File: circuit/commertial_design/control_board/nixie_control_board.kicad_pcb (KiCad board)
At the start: 2 copper layers, 200 x 65.3 mm, 75 parts, among them CON1 BARREL_JACK, IC1 ATMEGA328P-A, P1 CONN_01X08, P2 CONN_02X03, P3 CONN_01X12, P4 CONN_01X04, P5 BLUETOOTH_SJ, P6 CONN_02X03, Q1 2SB647, Q2 2SK3611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

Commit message: Add some marks
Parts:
- added REF**: Symbol_HighVoltage_Type2_CopperTop_VerySmall, warning:warning, B.Cu at (122.0, 124.3)
- added REF**: Pin_Header_Straight_2x03, Pin_Headers:Pin_Header_Straight_2x03, F.Cu at (178.0, 85.6)
- added REF**: Pin_Header_Straight_2x06, Pin_Headers:Pin_Header_Straight_2x06, F.Cu at (157.7, 85.6)
- added REF**: Pin_Header_Straight_2x04, Pin_Headers:Pin_Header_Straight_2x04, F.Cu at (142.4, 85.6)
- added REF**: Symbol_HighVoltage_Type2_CopperTop_VerySmall, warning:warning, F.Cu at (122.3, 125.5)
- moved C10 7.96 mm to (77.6, 106.9), turned to 90 degrees
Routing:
- net /power_supply/12V: track 61.5 -> 86.4 mm
- net Net-(P1-Pad5): track 17.8 -> 9.62 mm
- net /RTC/GND: track 894.3 -> 893.4 mm
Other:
- board text added: "Designed by Shengwen Cheng (2013 - 2016)"
- board text removed: "Designed by Shengwen Cheng"
- board text removed: "NIXIE CLOCK CONTROL BOARD"

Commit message: Push the forgotten file
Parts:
- removed R13, R14: 330ohm, Resistors_SMD:R_1206_HandSoldering
- removed the REF** at (122.0, 124.3)
- removed the REF** at (178.0, 85.6)
- removed the REF** at (122.3, 125.5)
- BT1: value CR1220 -> CR2032
- C6: value 33v/250v -> 33uf/250v
- P2: value CONN_02X03 -> CONN_02X01; footprint SMD_PIN_2_BY_3_REVERSE:SMD_PIN_2_BY_3_REVERSE -> Pin_Headers:Pin_Header_Straight_2x01
- Q3, Q4: value Q_NPN_EBC -> MPSA42
- R10: value R -> 33K ohm
- R11: value R -> 33k ohm
- R7: value 760 ohm -> 750 ohm
- R9: value 18k ohm -> 5.1k ohm
- moved R19 6.25 mm to (217.1, 113.5)
- moved R18 6.20 mm to (217.0, 111.1)
- moved C13 1.87 mm to (223.0, 110.2), turned to 270 degrees
- turned C15 to 0 degrees
- turned P2 to 90 degrees
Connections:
- IC1 pad 1: Search_button -> dfplayer_state
- IC1 pad 12: Digit_A0 -> MP3_RX
- IC1 pad 13: dfplayer_state -> MP3_TX
- IC1 pad 19: dfplayer_pre -> (no net)
- IC1 pad 2: Adjust_button -> (no net)
- IC1 pad 22: dfplayer_next -> (no net)
- IC1 pad 25: MP3_TX -> (no net)
- IC1 pad 26: MP3_RX -> Digit_A0
- R18 pad 2: MP3_RX -> MP3_TX
- R19 pad 2: MP3_TX -> MP3_RX
- U18 pad 11: dfplayer_pre -> (no net)
- U18 pad 9: dfplayer_next -> (no net)
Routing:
- net dfplayer_state: track 110.9 -> 42.2 mm, vias 2 -> 1
- net dfplayer_pre: track 67.3 -> 0.00 mm, vias 2 -> 0
- net dfplayer_next: track 56.4 -> 0.00 mm, vias 1 -> 0
- net Adjust_button: track 55.9 -> 0.00 mm, vias 2 -> 0
- net Search_button: track 53.9 -> 0.00 mm, vias 2 -> 0
- net MP3_RX: track 3.88 -> 22.4 mm, vias 0 -> 2
- net MP3_TX: track 4.61 -> 22.9 mm, vias 0 -> 2
- net Digit_A0: track 76.8 -> 91.8 mm, vias 1 -> 0
- net /RTC/I2C_SDA: track 51.8 -> 43.1 mm
- net /RTC/GND: track 893.4 -> 887.4 mm
- net /RTC/5V: track 367.9 -> 373.7 mm, vias 3 -> 5
- net Net-(R19-Pad1): track 13.3 -> 7.65 mm
- net Net-(R18-Pad1): track 13.3 -> 7.66 mm
- net Reset: track 58.8 -> 62.4 mm
- net left_comma: track 52.6 -> 55.1 mm, vias 1 -> 3
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
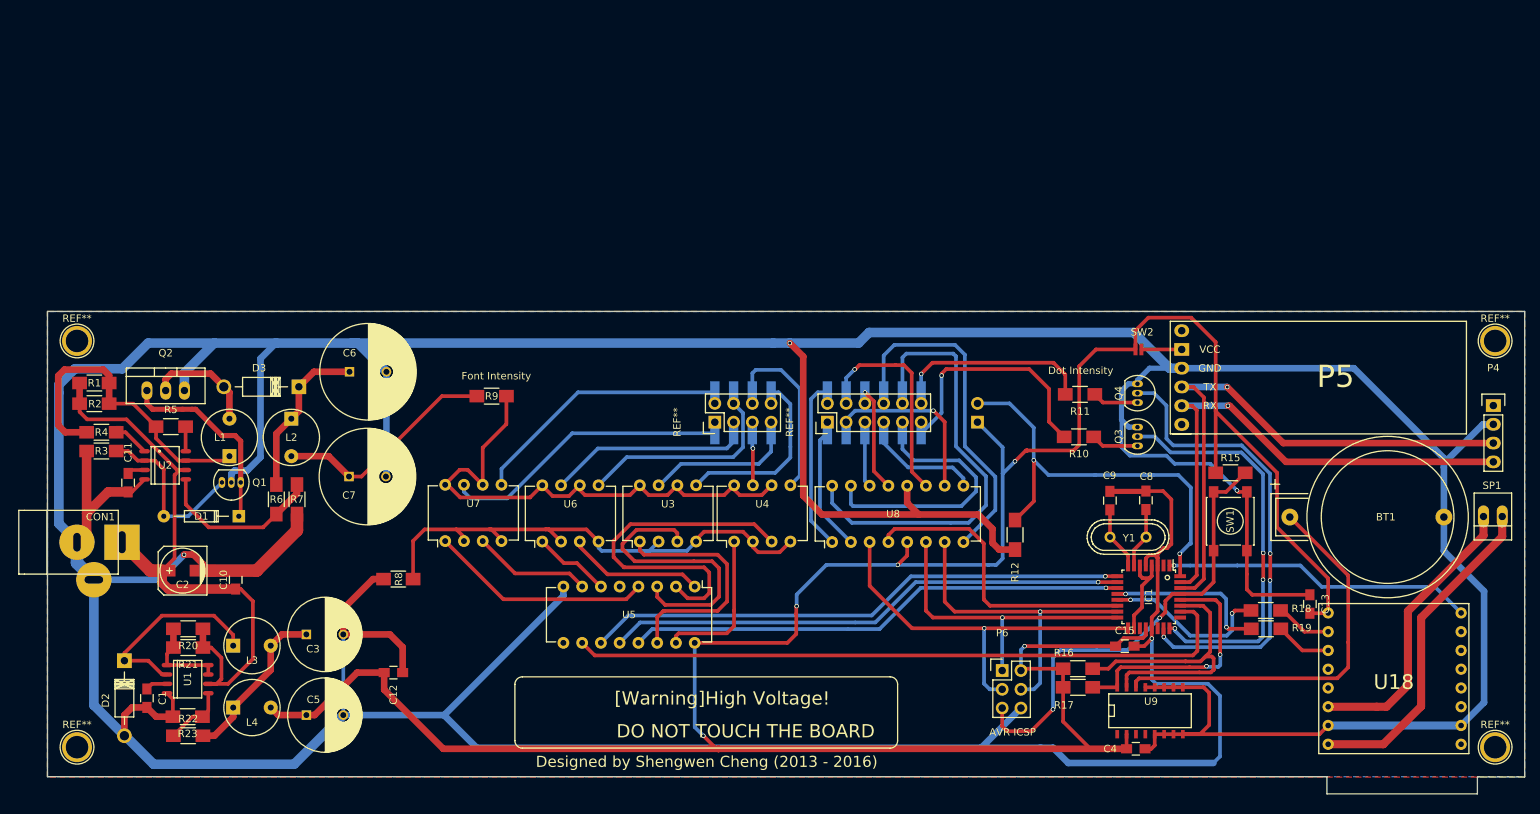
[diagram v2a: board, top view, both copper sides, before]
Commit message: Add ratio extender circuit
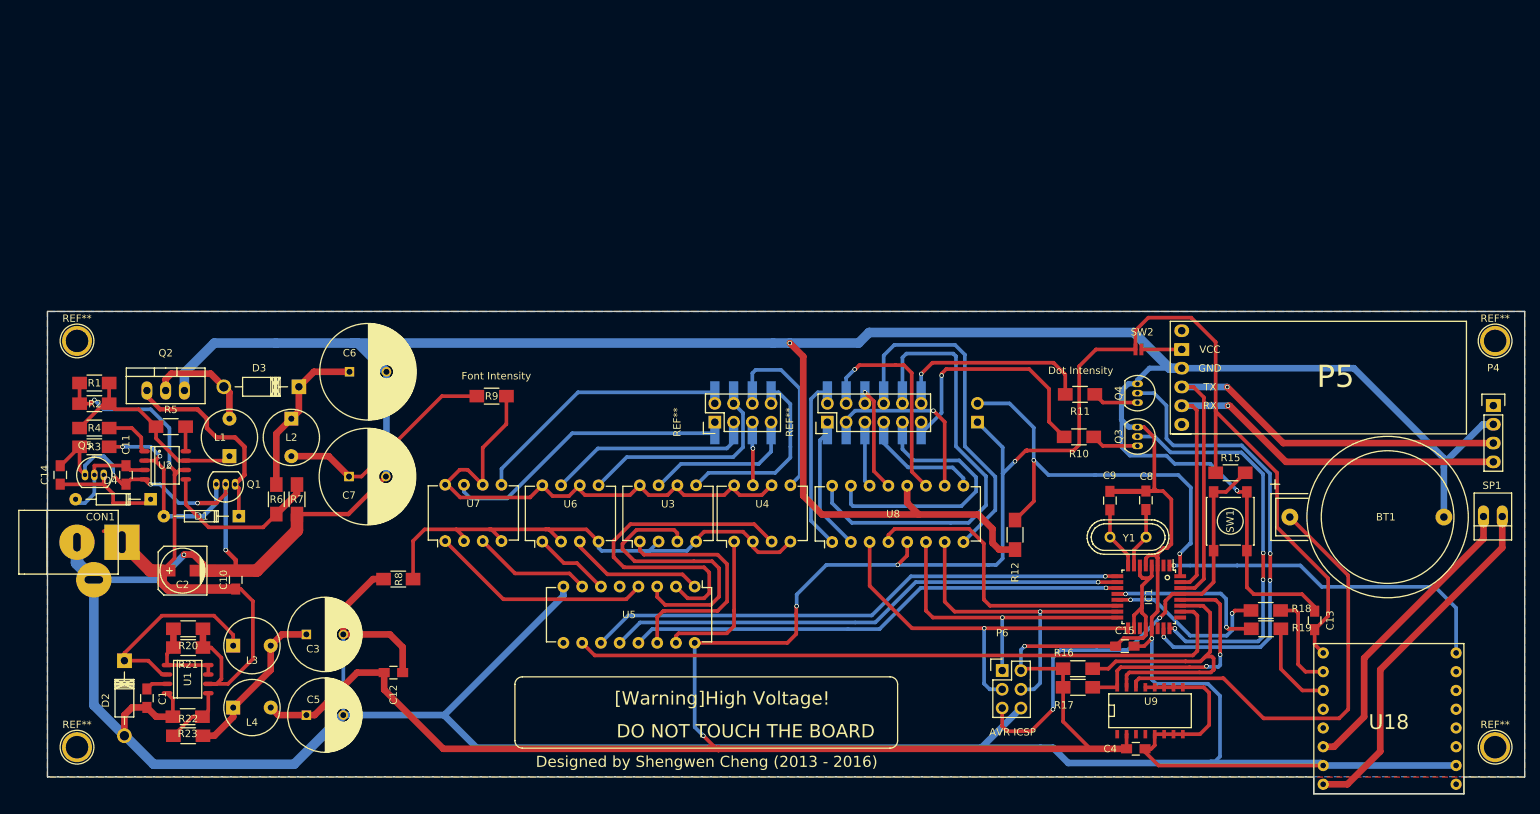
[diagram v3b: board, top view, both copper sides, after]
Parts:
- added C14: 330pf, Capacitors_SMD:C_0805_HandSoldering, F.Cu at (53.8, 92.7)
- added D4: D_Schottky, Diodes_ThroughHole:Diode_DO-35_SOD27_Horizontal_RM10, F.Cu at (66.0, 96.0)
- added Q5: BC557, TO_SOT_Packages_THT:TO-92_Inline_Narrow_Oval, F.Cu at (57.1, 92.7)
- moved U18 5.46 mm to (233.7, 125.7)
- moved C13 2.31 mm to (223.6, 112.4)
- moved R3 1.11 mm to (58.4, 88.9)
- moved R4 1.11 mm to (58.4, 86.4)
- moved C11 1.09 mm to (62.7, 92.7)
- moved Q1 0.80 mm to (77.5, 94.0)
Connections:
- C10 pad 2: /RTC/GND -> Net-(C10-Pad2)
- C11 pad 2: /RTC/GND -> Net-(C10-Pad2)
- C2 pad 2: /RTC/GND -> Net-(C10-Pad2)
- C6 pad 2: /RTC/GND -> Net-(C10-Pad2)
- C7 pad 2: /RTC/GND -> Net-(C10-Pad2)
- IC1 pad 19: (no net) -> Net-(IC1-Pad19)
- IC1 pad 2: (no net) -> Net-(IC1-Pad2)
- IC1 pad 22: (no net) -> Net-(IC1-Pad22)
- IC1 pad 25: (no net) -> Net-(IC1-Pad25)
- P4 pad 1: (no net) -> Net-(P4-Pad1)
- Q1 pad 2: /RTC/GND -> Net-(C10-Pad2)
- Q2 pad 3: /RTC/GND -> Net-(C10-Pad2)
- R3 pad 2: /RTC/GND -> Net-(C10-Pad2)
- R7 pad 2: /RTC/GND -> Net-(C10-Pad2)
- U18 pad 11: (no net) -> Net-(U18-Pad11)
- U18 pad 12: (no net) -> Net-(U18-Pad12)
- U18 pad 13: (no net) -> Net-(U18-Pad13)
- U18 pad 14: (no net) -> Net-(U18-Pad14)
- U18 pad 15: (no net) -> Net-(U18-Pad15)
- U18 pad 4: (no net) -> Net-(U18-Pad4)
- U18 pad 5: (no net) -> Net-(U18-Pad5)
- U18 pad 9: (no net) -> Net-(U18-Pad9)
- U2 pad 4: /RTC/GND -> Net-(C10-Pad2)
- U5 pad 5: (no net) -> Net-(U5-Pad5)
- U5 pad 9: (no net) -> Net-(U5-Pad9)
- U9 pad 1: (no net) -> Net-(U9-Pad1)
- U9 pad 3: (no net) -> Net-(U9-Pad3)
- U9 pad 4: (no net) -> Net-(U9-Pad4)
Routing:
- net /RTC/GND: track 887.4 -> 674.1 mm
- net Net-(C10-Pad2): track 0.00 -> 187.5 mm, vias 0 -> 4
- net Net-(C14-Pad1): track 0.00 -> 15.5 mm
- net Net-(L1-Pad1): track 43.0 -> 28.8 mm
- net Net-(C11-Pad1): track 2.41 -> 14.1 mm
- net Net-(BT1-Pad1): track 53.9 -> 61.8 mm
- net /RTC/5V: track 373.7 -> 381.2 mm
- net Net-(R18-Pad1): track 7.66 -> 13.6 mm
- net dfplayer_state: track 42.2 -> 47.3 mm
- net Net-(R19-Pad1): track 7.65 -> 12.4 mm
- net Net-(D1-Pad2): track 23.6 -> 28.2 mm, vias 0 -> 2
- net Net-(SP1-Pad1): track 45.0 -> 48.2 mm
- net Net-(SP1-Pad2): track 39.1 -> 41.0 mm
- net /power_supply/12V: track 86.4 -> 88.2 mm, vias 0 -> 2
- net Net-(R4-Pad2): track 5.57 -> 6.93 mm
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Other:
- outline, holes or cut-outs redrawn

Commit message: Update commertial board
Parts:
- added REF**: Symbol_HighVoltage_Type2_CopperTop_VerySmall, warning:warning, F.Cu at (121.9, 125.7)
- added REF**: Symbol_HighVoltage_Type2_CopperTop_VerySmall, warning:warning, B.Cu at (121.9, 124.5)
- moved P1 0.25 mm to (142.4, 85.3)
- moved P2 0.25 mm to (178.0, 85.3)
- moved P3 0.25 mm to (157.7, 85.3)
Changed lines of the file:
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@@
     (tracks 974)
     (zones 0)
-    (modules 78)
+    (modules 80)
     (nets 98)
   )
@@
   )
   (setup
-    (last_trace_width 0.5)
+    (last_trace_width 0.25)
     (user_trace_width 0.5)
     (user_trace_width 0.6)
@@
     (pad_to_mask_clearance 0.2)
     (aux_axis_origin 0 0)
-    (visible_elements FFFFEFFF)
+    (visible_elements FFFFFFFF)
     (pcbplotparams
       (layerselection 0x01030_80000001)
@@
   )
   (module SMD_PIN_2_BY_4_REVERSE:SMD_PIN_2_BY_4_REVERSE (layer B.Cu)
-    (at 142.42288 85.56244)
+    (at 142.42288 85.30844)
     (fp_text reference P1 (at 3.81 -6.985) (layer B.SilkS)
       (effects (font (size 1 1) (thickness 0.15)) (justify mirror))
@@
   )
   (module SMD_PIN_2_BY_6_REVERSE:SMD_PIN_2_BY_6_REVERSE (layer B.Cu)
-    (at 157.66288 85.56244)
+    (at 157.66288 85.30844)
     (fp_text reference P3 (at 6.35 4.445) (layer B.SilkS)
       (effects (font (size 1 1) (thickness 0.15)) (justify mirror))
@@
   )
   (module Pin_Headers:Pin_Header_Straight_2x01 (layer B.Cu)
-    (at 177.98288 85.56244 90)
+    (at 177.98288 85.30844 90)
     (descr "Through hole pin header")
     (tags "pin header")
@@
     )
   )
+  (module warning:warning (layer F.Cu)
+    (at 121.92 125.73)
+    (descr "Symbol, High Voltage, Type 2, Copper Top, Very Small,")
+    (tags "Symbol, High Voltage, Type 2, Copper Top, Very Small,")
+    (fp_text reference REF** (at -11.43 3.81) (layer F.SilkS)
+      (effects (font (size 1 1) (thickness 0.15)))
+    )
+    (fp_text value Symbol_HighVoltage_Type2_CopperTop_VerySmall (at 2.54 -10.16) (layer F.Fab)
+      (effects (font (size 1 1) (thickness 0.15)))
+    )
+    (fp_line (start -0.49784 2.19964) (end 0.70104 -0.89916) (layer F.SilkS) (width 0.381))
+    (fp_line (start 0.70104 -0.89916) (end 0.1016 -0.50038) (layer F.SilkS) (width 0.381))
+    (fp_line (start -0.89916 0.20066) (end 0.40132 -2.60096) (layer F.SilkS) (width 0.381))
+    (fp_line (start -0.49784 2.19964) (end 0.1016 1.50114) (layer F.SilkS) (width 0.381))
+    (fp_line (start -0.09906 -2.79908) (end -0.89916 0.20066) (layer F.SilkS) (width 0.381))
+    (fp_line (start -0.89916 0.20066) (end 0.29972 -0.59944) (layer F.SilkS) (width 0.381))
+    (fp_line (start 0.29972 -0.59944) (end -0.49784 2.19964) (layer F.SilkS) (width 0.381))
+    (fp_line (start -0.49784 2.19964) (end -0.59944 1.30048) (layer F.SilkS) (width 0.381))
+    (fp_line (start 0 -4.191) (end 4.699 2.794) (layer F.SilkS) (width 0.381))
+    (fp_line (start 4.699 2.794) (end -4.699 2.794) (layer F.SilkS) (width 0.381))
+    (fp_line (start -4.699 2.794) (end 0 -4.191) (layer F.SilkS) (width 0.381))
+  )
+  (module warning:warning (layer B.Cu)
+    (at 121.92 124.46)
+    (descr "Symbol, High Voltage, Type 2, Copper Top, Very Small,")
+    (tags "Symbol, High Voltage, Type 2, Copper Top, Very Small,")
+    (fp_text reference REF** (at -11.43 -3.81) (layer B.SilkS)
+      (effects (font (size 1 1) (thickness 0.15)) (justify mirror))
+    )
+    (fp_text value Symbol_HighVoltage_Type2_CopperTop_VerySmall (at 2.54 10.16) (layer B.Fab)
+      (effects (font (size 1 1) (thickness 0.15)) (justify mirror))
+    )
+    (fp_line (start -0.49784 -2.19964) (end 0.70104 0.89916) (layer B.SilkS) (width 0.381))
+    (fp_line (start 0.70104 0.89916) (end 0.1016 0.50038) (layer B.SilkS) (width 0.381))
+    (fp_line (start -0.89916 -0.20066) (end 0.40132 2.60096) (layer B.SilkS) (width 0.381))
+    (fp_line (start -0.49784 -2.19964) (end 0.1016 -1.50114) (layer B.SilkS) (width 0.381))
+    (fp_line (start -0.09906 2.79908) (end -0.89916 -0.20066) (layer B.SilkS) (width 0.381))
+    (fp_line (start -0.89916 -0.20066) (end 0.29972 0.59944) (layer B.SilkS) (width 0.381))
+    (fp_line (start 0.29972 0.59944) (end -0.49784 -2.19964) (layer B.SilkS) (width 0.381))
+    (fp_line (start -0.49784 -2.19964) (end -0.59944 -1.30048) (layer B.SilkS) (width 0.381))
+    (fp_line (start 0 4.191) (end 4.699 -2.794) (layer B.SilkS) (width 0.381))
+    (fp_line (start 4.699 -2.794) (end -4.699 -2.794) (layer B.SilkS) (width 0.381))
+    (fp_line (start -4.699 -2.794) (end 0 4.191) (layer B.SilkS) (width 0.381))
+  )
   (gr_circle (center 203.69276 106.59872) (end 203.91628 106.7943) (layer F.SilkS) (width 0.15))
   (gr_text "Designed by Shengwen Cheng (2013 - 2016)" (at 141.59992 118.4656 180) (layer B.SilkS)
@@
   (segment (start 73.12 113.538) (end 73.12 116.078) (width 0.9) (layer F.Cu) (net 2))
   (segment (start 200.26122 110.49) (end 200.26122 111.36122) (width 0.5) (layer F.Cu) (net 3))
-  (segment (start 200.77435 111.87435) (end 200.77435 113.46873) (width 0.5) (layer F.Cu) (net 3) (status 800000))
+  (segment (start 200.77435 111.87435) (end 200.77435 113.46873) (width 0.5) (layer F.Cu) (net 3))
   (segment (start 200.26122 111.36122) (end 200.77435 111.87435) (width 0.5) (layer F.Cu) (net 3))
   (segment (start 225.4631 111.28502) (end 225.4631 111.82128) (width 0.5) (layer F.Cu) (net 3))
@@
   (segment (start 198.37435 104.96873) (end 198.37435 103.56631) (width 0.5) (layer F.Cu) (net 7))
   (segment (start 198.37435 103.56631) (end 195.92925 101.12121) (width 0.5) (layer F.Cu) (net 7))
-  (segment (start 74.93 93.98) (end 74.93 96.52) (width 0.6) (layer B.Cu) (net 8) (status 400000))
-  (segment (start 73.14946 98.30054) (end 67.81748 98.30054) (width 0.6) (layer B.Cu) (net 8) (status 800000))
+  (segment (start 74.93 93.98) (end 74.93 96.52) (width 0.6) (layer B.Cu) (net 8))
+  (segment (start 73.14946 98.30054) (end 67.81748 98.30054) (width 0.6) (layer B.Cu) (net 8))
   (segment (start 74.93 96.52) (end 73.14946 98.30054) (width 0.6) (layer B.Cu) (net 8))
   (segment (start 66.63944 90.76944) (end 67.23888 90.17) (width 0.5) (layer F.Cu) (net 8))
@@
   (segment (start 67.81748 91.94748) (end 67.81748 98.30054) (width 0.5) (layer F.Cu) (net 8))
   (segment (start 66.63944 90.76944) (end 67.81748 91.94748) (width 0.5) (layer F.Cu) (net 8))
-  (segment (start 77.47 93.98) (end 78.74 92.71) (width 0.6) (layer F.Cu) (net 9) (status 400000))
-  (segment (start 67.31 83.82) (end 65.532 82.042) (width 0.6) (layer F.Cu) (net 9) (status 800000))
+  (segment (start 77.47 93.98) (end 78.74 92.71) (width 0.6) (layer F.Cu) (net 9))
+  (segment (start 67.31 83.82) (end 65.532 82.042) (width 0.6) (layer F.Cu) (net 9))
   (segment (start 72.39 83.82) (end 67.31 83.82) (width 0.6) (layer F.Cu) (net 9))
   (segment (start 73.66 85.09) (end 72.39 83.82) (width 0.6) (layer F.Cu) (net 9))
@@
   (segment (start 78.74 88.9) (end 77.47 87.63) (width 0.6) (layer F.Cu) (net 9))
   (segment (start 78.74 92.71) (end 78.74 88.9) (width 0.6) (layer F.Cu) (net 9))
-  (segment (start 65.532 82.042) (end 65.532 81.28) (width 0.6) (layer F.Cu) (net 9) (status C00000))
+  (segment (start 65.532 82.042) (end 65.532 81.28) (width 0.6) (layer F.Cu) (net 9))
   (segment (start 77.97748 94.48748) (end 77.97748 98.30054) (width 0.5) (layer F.Cu) (net 9))
   (segment (start 77.47 93.98) (end 77.97748 94.48748) (width 0.5) (layer F.Cu) (net 9))
@@
   (segment (start 199.4408 121.46026) (end 199.4408 120.67032) (width 0.5) (layer F.Cu) (net 77))
   (segment (start 228.17887 106.31881) (end 220.27236 98.4123) (width 0.5) (layer F.Cu) (net 77))
-  (segment (start 85.852 98.012) (end 92.80932 98.012) (width 0.6) (layer F.Cu) (net 78) (status 400000))
-  (segment (start 92.80932 98.012) (end 97.89288 92.92844) (width 0.6) (layer F.Cu) (net 78) (status 800000))
-  (segment (start 77.55636 105.6586) (end 77.55636 104.22636) (width 0.6) (layer F.Cu) (net 78) (status 400000))
-  (segment (start 76.2 102.87) (end 76.2 93.98) (width 0.6) (layer B.Cu) (net 78) (status 800000))
+  (segment (start 85.852 98.012) (end 92.80932 98.012) (width 0.6) (layer F.Cu) (net 78))
+  (segment (start 92.80932 98.012) (end 97.89288 92.92844) (width 0.6) (layer F.Cu) (net 78))
+  (segment (start 77.55636 105.6586) (end 77.55636 104.22636) (width 0.6) (layer F.Cu) (net 78))
+  (segment (start 76.2 102.87) (end 76.2 93.98) (width 0.6) (layer B.Cu) (net 78))
   (via (at 76.2 102.87) (size 0.6) (drill 0.4) (layers F.Cu B.Cu) (net 78))
   (segment (start 77.55636 104.22636) (end 76.2 102.87) (width 0.6) (layer F.Cu) (net 78))
@@
       (pts
         (xy 235.89488 133.82244) (xy 211.51088 133.82244) (xy 211.51088 135.34644) (xy 190.17488 135.34644) (xy 190.17488 133.82244)
-        (xy 51.99888 133.82244) (xy 51.99888 75.91044) (xy 235.89488 75.91044) (xy 235.89488 133.82244)
+        (xy 51.99888 133.82244) (xy 51.99888 75.91044) (xy 235.89488 75.91044)
       )
     )
@@
     (polygon
       (pts
-        (xy 228.27488 132.29844) (xy 213.03488 132.29844) (xy 213.03488 107.40644) (xy 228.27488 107.40644) (xy 228.27488 132.29844)
+        (xy 228.27488 132.29844) (xy 213.03488 132.29844) (xy 213.03488 107.40644) (xy 228.27488 107.40644)
       )
     )
@@
     (polygon
       (pts
-        (xy 228.27488 132.29844) (xy 213.03488 132.29844) (xy 213.03488 107.40644) (xy 228.27488 107.40644) (xy 228.27488 132.29844)
+        (xy 228.27488 132.29844) (xy 213.03488 132.29844) (xy 213.03488 107.40644) (xy 228.27488 107.40644)
       )
     )
@@
     (polygon
       (pts
-        (xy 244.17782 87.13724) (xy 238.71428 87.13724) (xy 238.71428 71.95566) (xy 244.17782 71.95566) (xy 244.17782 87.13724)
+        (xy 244.17782 87.13724) (xy 238.71428 87.13724) (xy 238.71428 71.95566) (xy 244.17782 71.95566)
       )
     )

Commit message: Update commertial board
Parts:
- removed the REF** at (142.4, 85.6)
- removed the REF** at (157.7, 85.6)
- P1: footprint SMD_PIN_2_BY_4_REVERSE:SMD_PIN_2_BY_4_REVERSE -> Pin_Headers:Pin_Header_Straight_2x04; moved to F.Cu
- P3: footprint SMD_PIN_2_BY_6_REVERSE:SMD_PIN_2_BY_6_REVERSE -> Pin_Headers:Pin_Header_Straight_2x06; moved to F.Cu
- turned P1 to 90 degrees
- turned P3 to 90 degrees
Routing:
- net Net-(C10-Pad2): track 187.5 -> 131.1 mm
- net Net-(P3-Pad6): track 14.0 -> 32.1 mm
- net Net-(P3-Pad4): track 28.1 -> 40.6 mm, vias 1 -> 0
- net Net-(P3-Pad3): track 25.0 -> 20.3 mm, vias 1 -> 0
- net _cathode_comma_right: track 26.0 -> 29.7 mm
- net Net-(P1-Pad3): track 27.0 -> 30.6 mm
- net Net-(P1-Pad4): track 29.7 -> 32.6 mm
- net Net-(P3-Pad7): track 15.1 -> 17.4 mm
- net Net-(P1-Pad5): track 7.40 -> 9.72 mm
- net Net-(P3-Pad5): track 7.37 -> 9.70 mm
- net Net-(P3-Pad9): track 36.0 -> 38.3 mm
- net Net-(P1-Pad7): track 19.6 -> 21.9 mm
- net /RTC/GND: track 674.1 -> 671.8 mm, vias 4 -> 3
- net Net-(P3-Pad1): track 16.9 -> 18.6 mm
- net Net-(P1-Pad1): track 38.9 -> 40.6 mm
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
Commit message: Fix PCB board
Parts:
- removed C11: 330pf, Capacitors_SMD:C_0805_HandSoldering
- U8: value K155ID1 -> 74L147
- U9: footprint SMD_Packages:SO-16-N -> SMD_Packages:SO-16-W
- moved C4 7.65 mm to (191.8, 129.5)
- moved U18 5.82 mm to (227.9, 126.4)
- moved U9 1.73 mm to (201.3, 126.4)
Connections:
- C10 pad 2: Net-(C10-Pad2) -> /RTC/GND
- C14 pad 2: Net-(C10-Pad2) -> /RTC/GND
- C2 pad 2: Net-(C10-Pad2) -> /RTC/GND
- C6 pad 2: Net-(C10-Pad2) -> /RTC/GND
- C7 pad 2: Net-(C10-Pad2) -> /RTC/GND
- Q1 pad 2: Net-(C10-Pad2) -> /RTC/GND
- Q2 pad 3: Net-(C10-Pad2) -> /RTC/GND
- Q5 pad 1: Net-(C10-Pad2) -> /RTC/GND
- R3 pad 2: Net-(C10-Pad2) -> /RTC/GND
- R7 pad 2: Net-(C10-Pad2) -> /RTC/GND
- U2 pad 4: Net-(C10-Pad2) -> /RTC/GND
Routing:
- net /RTC/GND: track 671.8 -> 811.5 mm, vias 3 -> 7
- net Net-(C10-Pad2): track 131.1 -> 0.00 mm, vias 4 -> 0
- net Net-(SP1-Pad1): track 48.2 -> 61.3 mm
- net Net-(SP1-Pad2): track 41.0 -> 54.1 mm
- net dfplayer_state: track 47.3 -> 42.3 mm
- net Net-(R18-Pad1): track 13.6 -> 17.6 mm
- net /RTC/5V: track 381.2 -> 380.3 mm
- net Net-(R19-Pad1): track 12.4 -> 13.3 mm
- net Net-(BT1-Pad1): track 61.8 -> 62.6 mm
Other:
- board size 200 x 65.3 mm -> 200 x 66 mm
- board text added: "Designed by Shengwen Cheng"
- board text removed: "Designed by Shengwen Cheng (2013 - 2016)"
